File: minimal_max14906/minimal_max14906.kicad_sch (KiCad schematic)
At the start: 56 parts, among them Q1 SI7309DN-T1-E3, Q2 SI7309DN-T1-E3, Q3 SI7309DN-T1-E3, Q4 SI7309DN-T1-E3, U1 MAX14906ATM+

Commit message: minor updates
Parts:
- U1: MPN (none) -> MAX14906ATM+
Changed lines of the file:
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@@
+			)
+		)
+		(property "MPN" "MAX14906ATM+"
+			(at 167.64 152.4 0)
+			(effects
+				(font
+					(size 1.27 1.27)
+				)
+				(justify left)
+				(hide yes)
 			)
 		)

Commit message: Minor updates
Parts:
- added J1, J2, J3, J4: CLP-102-02-G-D-BE, connector_footprints:CLP-102-02-G-D-BE, symbol UNITED_CONNECTORS_DATA_BASE:J_CLP-102-02-G-D-BE
- added J5: CLP-114-02-G-D-BE, connector_footprints:CLP-114-02-G-D-BE, symbol UNITED_CONNECTORS_DATA_BASE:J_CLP-114-02-G-D-BE
- added J6, J7: CLP-104-02-G-D-BE, connector_footprints:CLP-104-02-G-D-BE, symbol UNITED_CONNECTORS_DATA_BASE:J_CLP-104-02-G-D-BE
- added TP25, TP26: TestPoint, test_point_footprints:TestPoint_THTPad_Castelated, symbol UNITED_TEST_POINTS:TestPoint_Castelated
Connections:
- net 3V3: now also J5.17, J5.18
- net CHANNEL_1: now also J4.3, J4.4
- net CHANNEL_2: now also J3.1, J3.2
- net CHANNEL_3: now also J2.3, J2.4
- net CHANNEL_4: now also J1.1, J1.2
- net CLK: now also J5.11, J5.12
- net D1: now also J5.25, J5.26
- net D2: now also J5.27, J5.28
- net D3: now also J5.1, J5.2
- net D4: now also J5.3, J5.4
- net EN: now also J5.21, J5.22
- net GNDA: now also J1.3, J1.4, J2.1, J2.2, J3.3, J3.4, J4.1, J4.2, J5.15, J5.16, J6.1, J6.2, J7.7, J7.8, TP26.1
- net SDI: now also J5.7, J5.8
- net SDO: now also J5.13, J5.14
- net SYNCH: now also J5.5, J5.6
- net VDD_24V_MAX14906: now also J6.3, J6.4, J7.5, J7.6, TP25.1
- net ~{CS}: now also J5.10, J5.9
- net ~{FAULT}: now also J5.19, J5.20
- net ~{READY}: now also J5.23, J5.24
- no-connect marks 1 -> 9
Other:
- moved on the sheet: C1, C10, C11, C12, C13, C2, C3, C4, C5, C6, C7, C8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

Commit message: Update subproject commit for KiCAD Symbol Generator
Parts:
- renumbered C5 to C1, C12 to C10, C7 to C11, C6 to C12, C9 to C13, C8 to C2, C2 to C3, C13 to C4, C4 to C5, C11 to C6, C3 to C7, C10 to C8, C1 to C9, D9 to D1, D8 to D2, D4 to D3, D7 to D4, D3 to D5, D2 to D7, D5 to D8, D1 to D9, J5 to J1, J7 to J4, J6 to J5, J1 to J6, J4 to J7, Q2 to Q1, Q4 to Q2, Q1 to Q3, Q3 to Q4, R5 to R1, R4 to R2, R2 to R4, R1 to R5, TP12 to TP1, TP8 to TP10, TP9 to TP11, TP10 to TP12, TP14 to TP13, TP13 to TP14, TP22 to TP15, TP23 to TP16, TP19 to TP17, TP25 to TP19, TP11 to TP2, TP15 to TP20, TP26 to TP21, TP16 to TP22, TP20 to TP23, TP17 to TP24, TP21 to TP25, TP24 to TP26, TP7 to TP3, TP6 to TP4, TP4 to TP6, TP3 to TP7, TP2 to TP8, TP1 to TP9

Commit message: Minor updates to project files
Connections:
- net 3V3: no longer J1.17
- net CLK: no longer J1.11
- net D1: no longer J1.25
- net D2: no longer J1.27
- net D3: no longer J1.1
- net D4: no longer J1.3
- net EN: no longer J1.21
- net GNDA: now also J1.1, J1.11, J1.13, J1.17, J1.19, J1.21, J1.23, J1.25, J1.27, J1.3, J1.5, J1.7, J1.9
- net SDI: no longer J1.7
- net SDO: no longer J1.13
- net SYNCH: no longer J1.5
- net ~{CS}: no longer J1.9
- net ~{FAULT}: no longer J1.19
- net ~{READY}: no longer J1.23

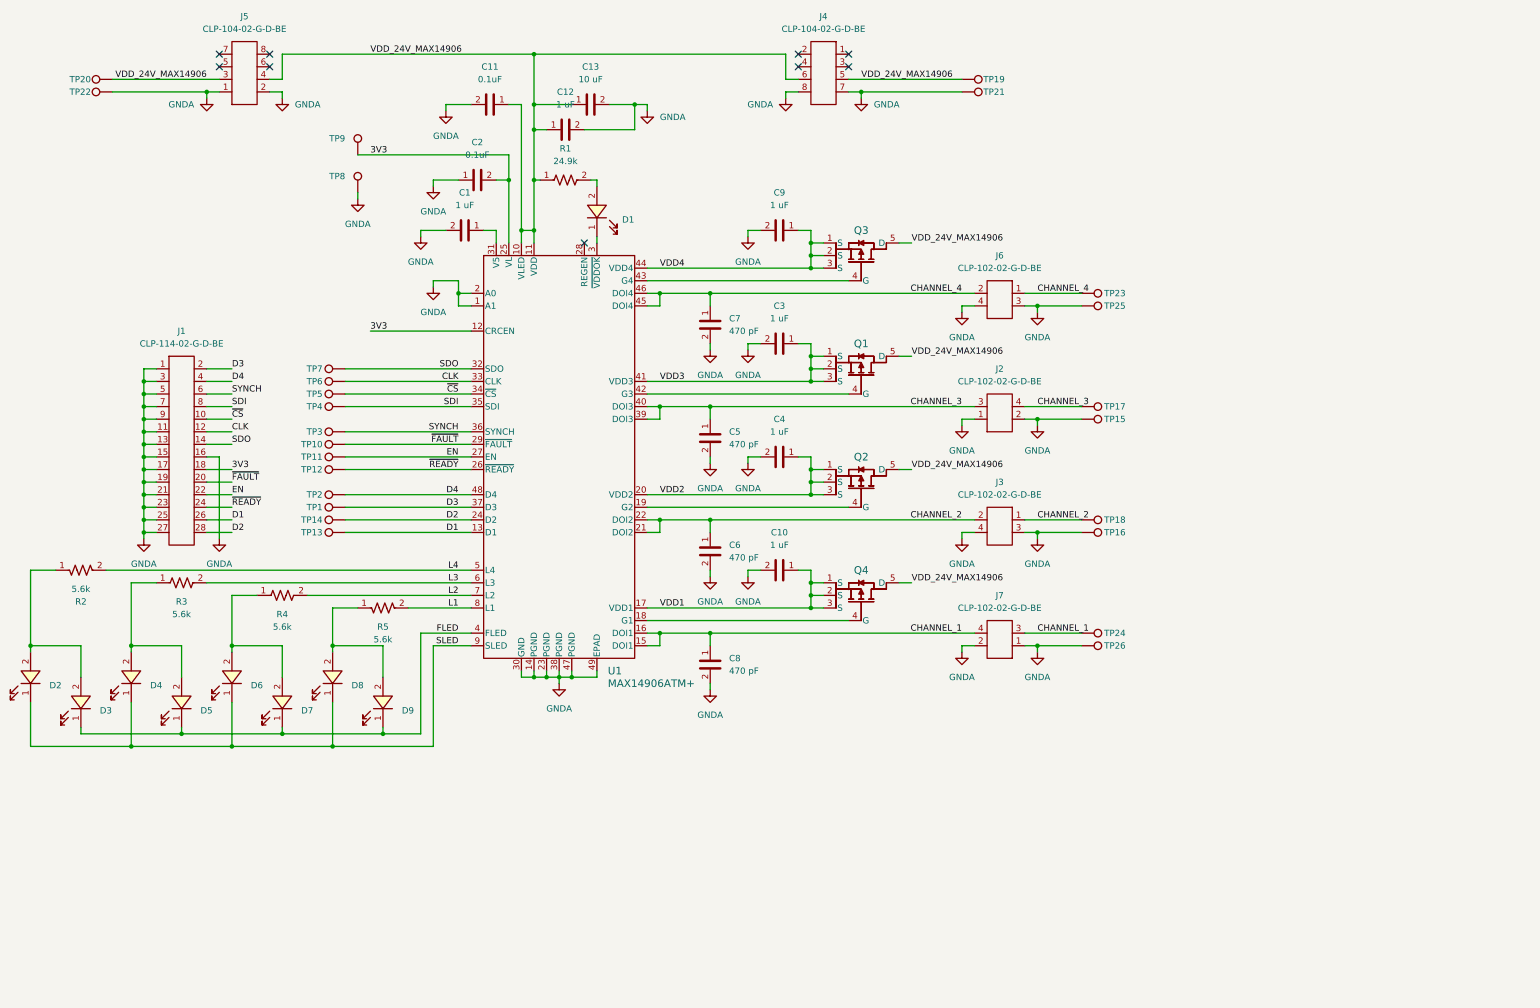
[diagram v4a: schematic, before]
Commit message: Update KiCAD Symbol Generator and configuration files
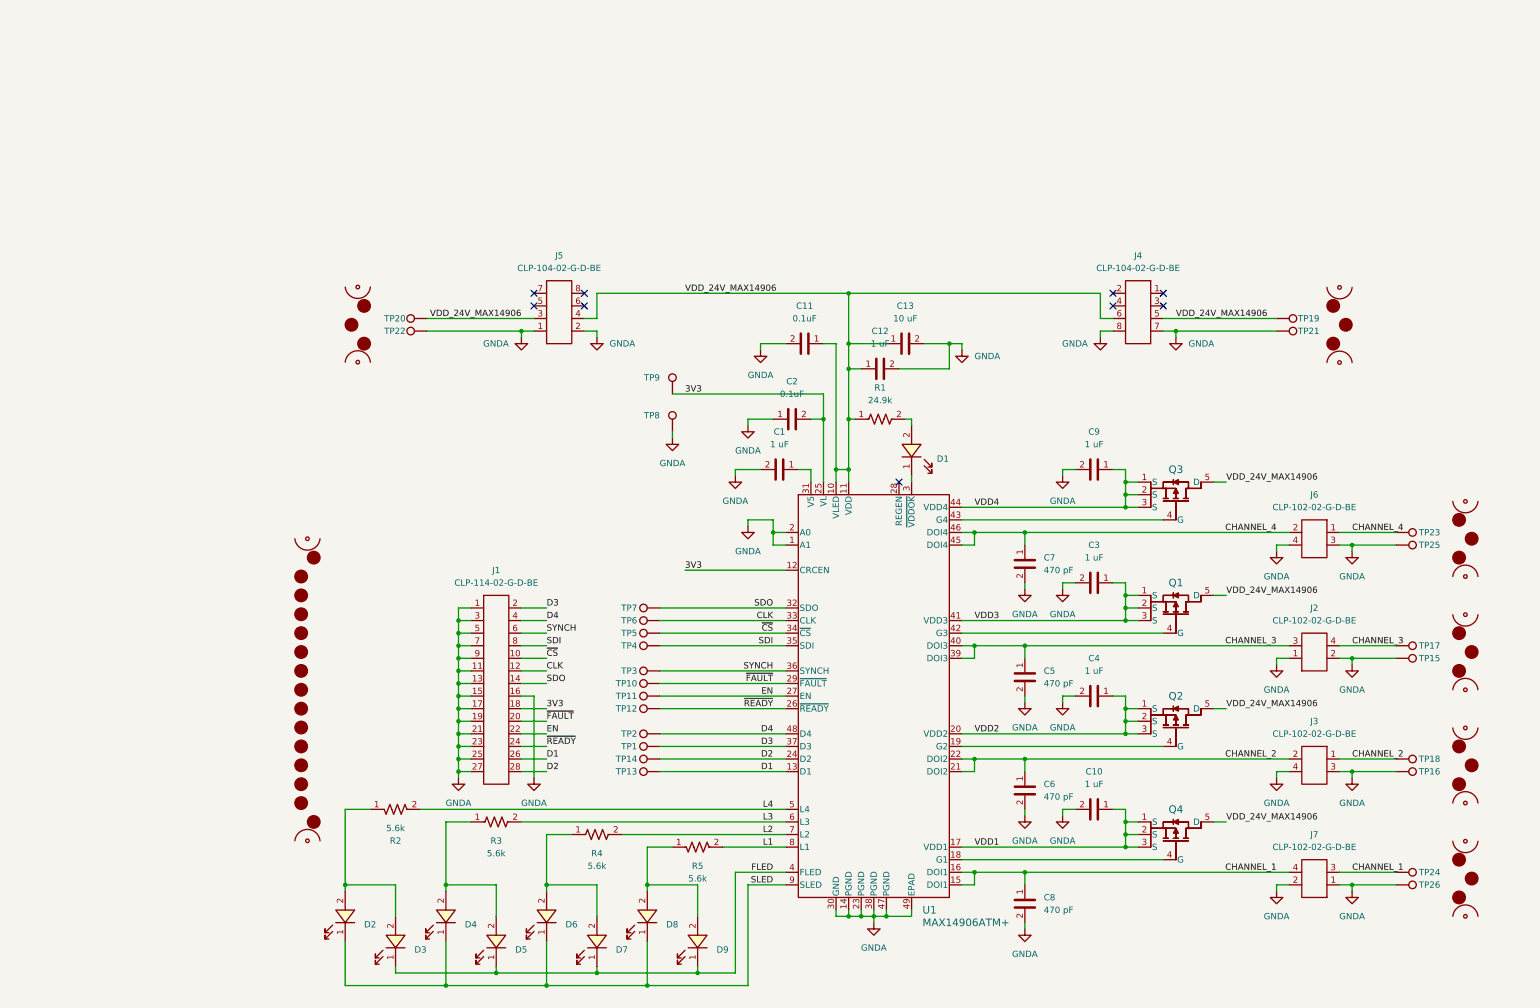
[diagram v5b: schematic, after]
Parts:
- added MB1, MB2, MB3, MB4, MB6, MB7: mouse-bite-midle-50mil-200mil, mouse_bite_footprints:mouse-bite-midle-50mil-200mil, symbol UNITED_MOUSE_BITES_DATA_BASE:mouse-bite-midle-50mil-200mil
- added MB5: mouse-bite-midle-50mil-200mil, mouse_bite_footprints:mouse-bite-50mil-790mil, symbol UNITED_MOUSE_BITES_DATA_BASE:mouse-bite-50mil-790mil
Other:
- moved on the sheet: C1, C10, C11, C12, C13, C2, C3, C4, C5, C6, C7, C8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

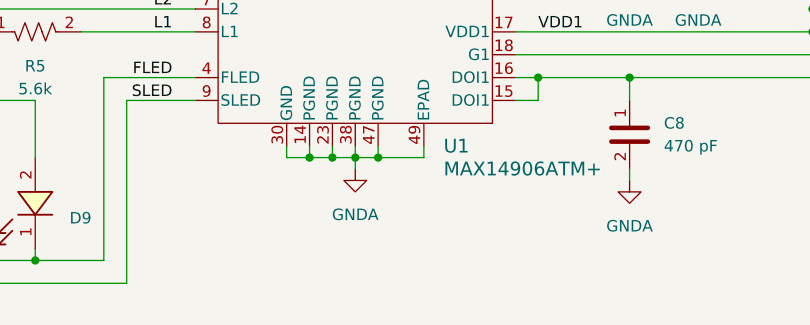
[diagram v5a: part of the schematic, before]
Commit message: Update KiCAD Symbol Generator subproject and add new footprints for fiducial markers
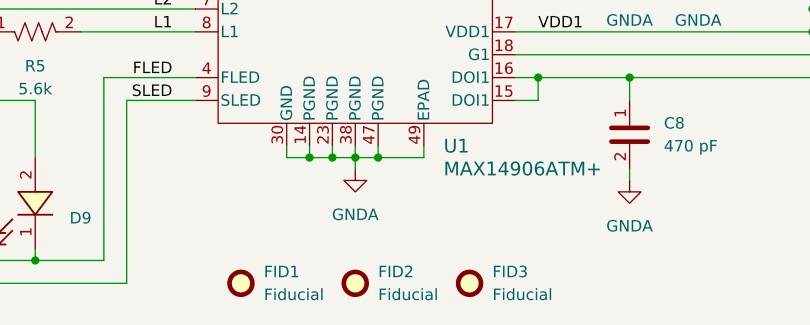
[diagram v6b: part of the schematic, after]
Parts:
- added FID1, FID2, FID3: Fiducial, no_components_footprints:Fiducial_0.5mm_Mask1mm, symbol UNITED_NO_COMPONENTS_DATA_BASE:Fiducial
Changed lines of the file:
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@@
 	)
 	(symbol
+		(lib_id "UNITED_NO_COMPONENTS_DATA_BASE:Fiducial")
+		(at 228.6 210.82 0)
+		(unit 1)
+		(exclude_from_sim no)
+		(in_bom yes)
+		(on_board yes)
+		(dnp no)
+		(fields_autoplaced yes)
+		(property "Reference" "FID3"
+			(at 231.14 209.5499 0)
+			(effects
+				(font
+					(size 1.27 1.27)
+				)
+				(justify left)
+			)
+		)
+		(property "Value" "Fiducial"
+			(at 231.14 212.0899 0)
+			(effects
+				(font
+					(size 1.27 1.27)
+				)
+				(justify left)
+			)
+		)
+		(property "Footprint" "no_components_footprints:Fiducial_0.5mm_Mask1mm"
+			(at 228.6 218.44 0)
+			(effects
+				(font
+					(size 1.27 1.27)
+				)
+				(justify left)
+				(hide yes)
+			)
+		)
+		(property "Datasheet" "~"
+			(at 228.6 213.36 0)
+			(effects
+				(font
+					(size 1.27 1.27)
+				)
+				(justify left)
+				(hide yes)
+			)
+		)
+		(property "Description" "Fiducial Marker"
+			(at 228.6 215.9 0)
+			(effects
+				(font
+					(size 1.27 1.27)
+				)
+				(justify left)
+				(hide yes)
+			)
+		)
+		(instances
+			(project "minimal_max14906"
+				(path "/0138bc01-efaa-4f20-bf65-043bbc1a8346"
+					(reference "FID3")
+					(unit 1)
+				)
+			)
+		)
+	)
+	(symbol
 		(lib_id "UNITED_DIODES_DATA_BASE:D_APHHS1005CGCK")
 		(at 109.22 196.85 90)
@@
 	)
 	(symbol
+		(lib_id "UNITED_NO_COMPONENTS_DATA_BASE:Fiducial")
+		(at 215.9 210.82 0)
+		(unit 1)
+		(exclude_from_sim no)
+		(in_bom yes)
+		(on_board yes)
+		(dnp no)
+		(fields_autoplaced yes)
+		(property "Reference" "FID2"
+			(at 218.44 209.5499 0)
+			(effects
+				(font
+					(size 1.27 1.27)
+				)
+				(justify left)
+			)
+		)
+		(property "Value" "Fiducial"
+			(at 218.44 212.0899 0)
+			(effects
+				(font
+					(size 1.27 1.27)
+				)
+				(justify left)
+			)
+		)
+		(property "Footprint" "no_components_footprints:Fiducial_0.5mm_Mask1mm"
+			(at 215.9 218.44 0)
+			(effects
+				(font
+					(size 1.27 1.27)
+				)
+				(justify left)
+				(hide yes)
+			)
+		)
+		(property "Datasheet" "~"
+			(at 215.9 213.36 0)
+			(effects
+				(font
+					(size 1.27 1.27)
+				)
+				(justify left)
+				(hide yes)
+			)
+		)
+		(property "Description" "Fiducial Marker"
+			(at 215.9 215.9 0)
+			(effects
+				(font
+					(size 1.27 1.27)
+				)
+				(justify left)
+				(hide yes)
+			)
+		)
+		(instances
+			(project "minimal_max14906"
+				(path "/0138bc01-efaa-4f20-bf65-043bbc1a8346"
+					(reference "FID2")
+					(unit 1)
+				)
+			)
+		)
+	)
+	(symbol
 		(lib_id "power:GNDA")
 		(at 297.18 146.05 0)
@@
 					(unit 1)
 				)
+			)
+		)
+	)
+	(symbol
+		(lib_id "UNITED_NO_COMPONENTS_DATA_BASE:Fiducial")
+		(at 203.2 210.82 0)
+		(unit 1)
+		(exclude_from_sim no)
+		(in_bom yes)
+		(on_board yes)
+		(dnp no)
+		(fields_autoplaced yes)
+		(property "Reference" "FID1"
+			(at 205.74 209.5499 0)
+			(effects
+				(font
+					(size 1.27 1.27)
+				)
+				(justify left)
+			)
+		)
+		(property "Value" "Fiducial"
+			(at 205.74 212.0899 0)
+			(effects
+				(font
+					(size 1.27 1.27)
+				)
+				(justify left)
+			)
+		)
+		(property "Footprint" "no_components_footprints:Fiducial_0.5mm_Mask1mm"
+			(at 203.2 218.44 0)
+			(effects
+				(font
+					(size 1.27 1.27)
+				)
+				(justify left)
+				(hide yes)
+			)
+		)
+		(property "Datasheet" "~"
+			(at 203.2 213.36 0)
+			(effects
+				(font
+					(size 1.27 1.27)
+				)
+				(justify left)
+				(hide yes)
+			)
+		)
+		(property "Description" "Fiducial Marker"
+			(at 203.2 215.9 0)
+			(effects
+				(font
+					(size 1.27 1.27)
+				)
+				(justify left)
+				(hide yes)
+			)
+		)
+		(instances
+			(project ""
+				(path "/0138bc01-efaa-4f20-bf65-043bbc1a8346"
+					(reference "FID1")
+					(unit 1)
+				)

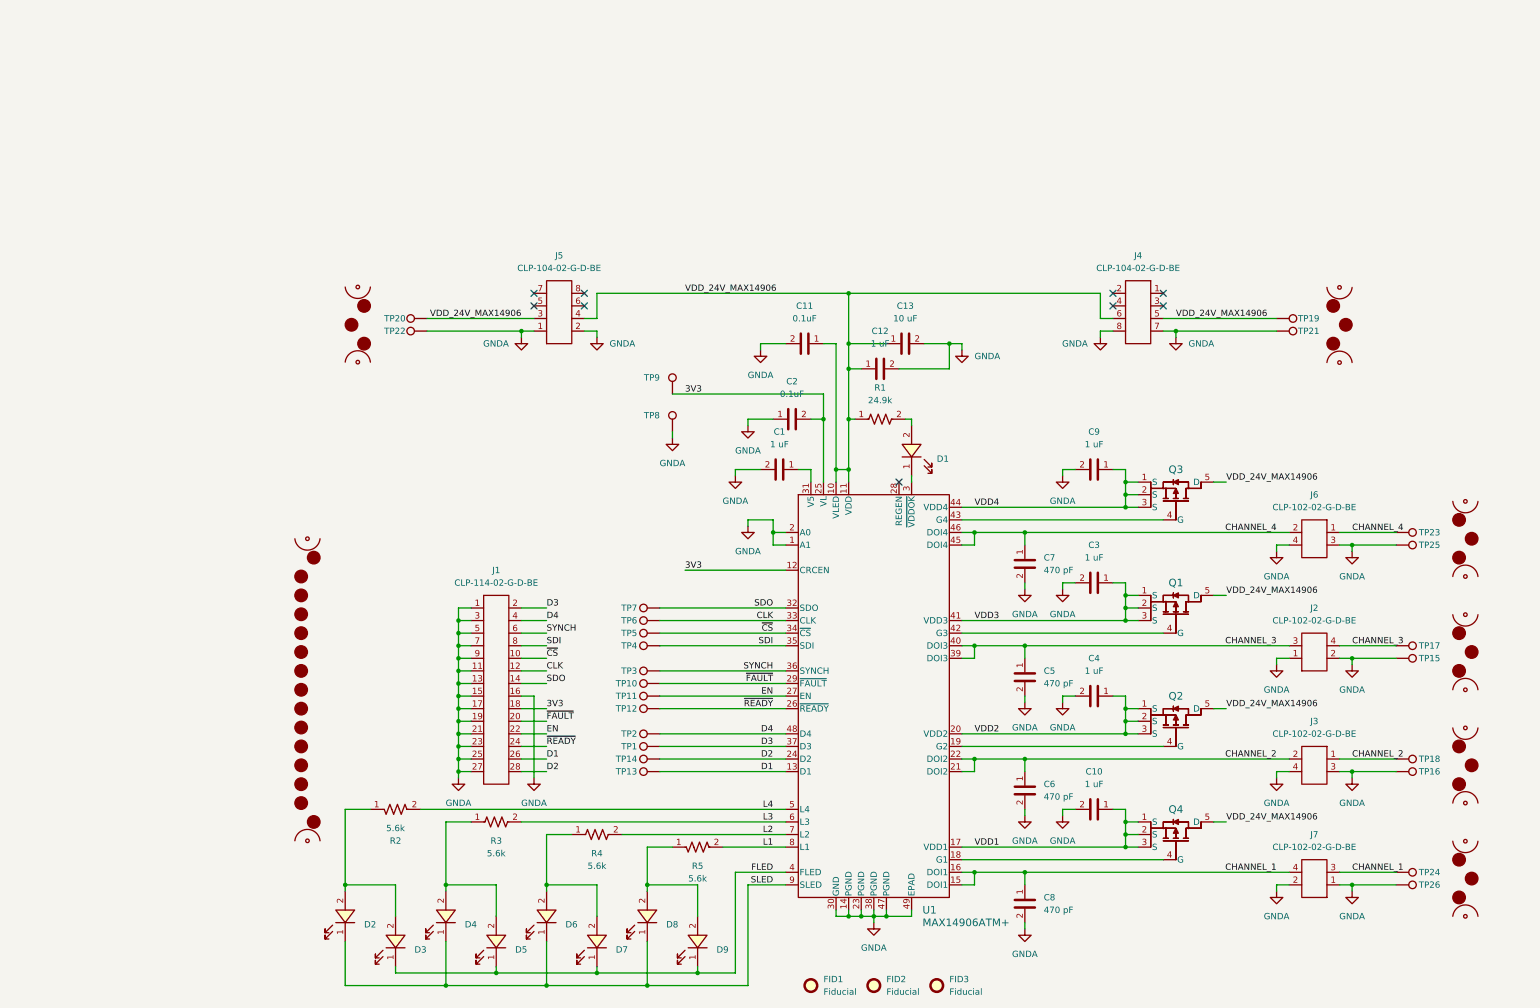
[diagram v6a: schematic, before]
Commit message: Update KiCAD Symbol Generator with new features and improvements
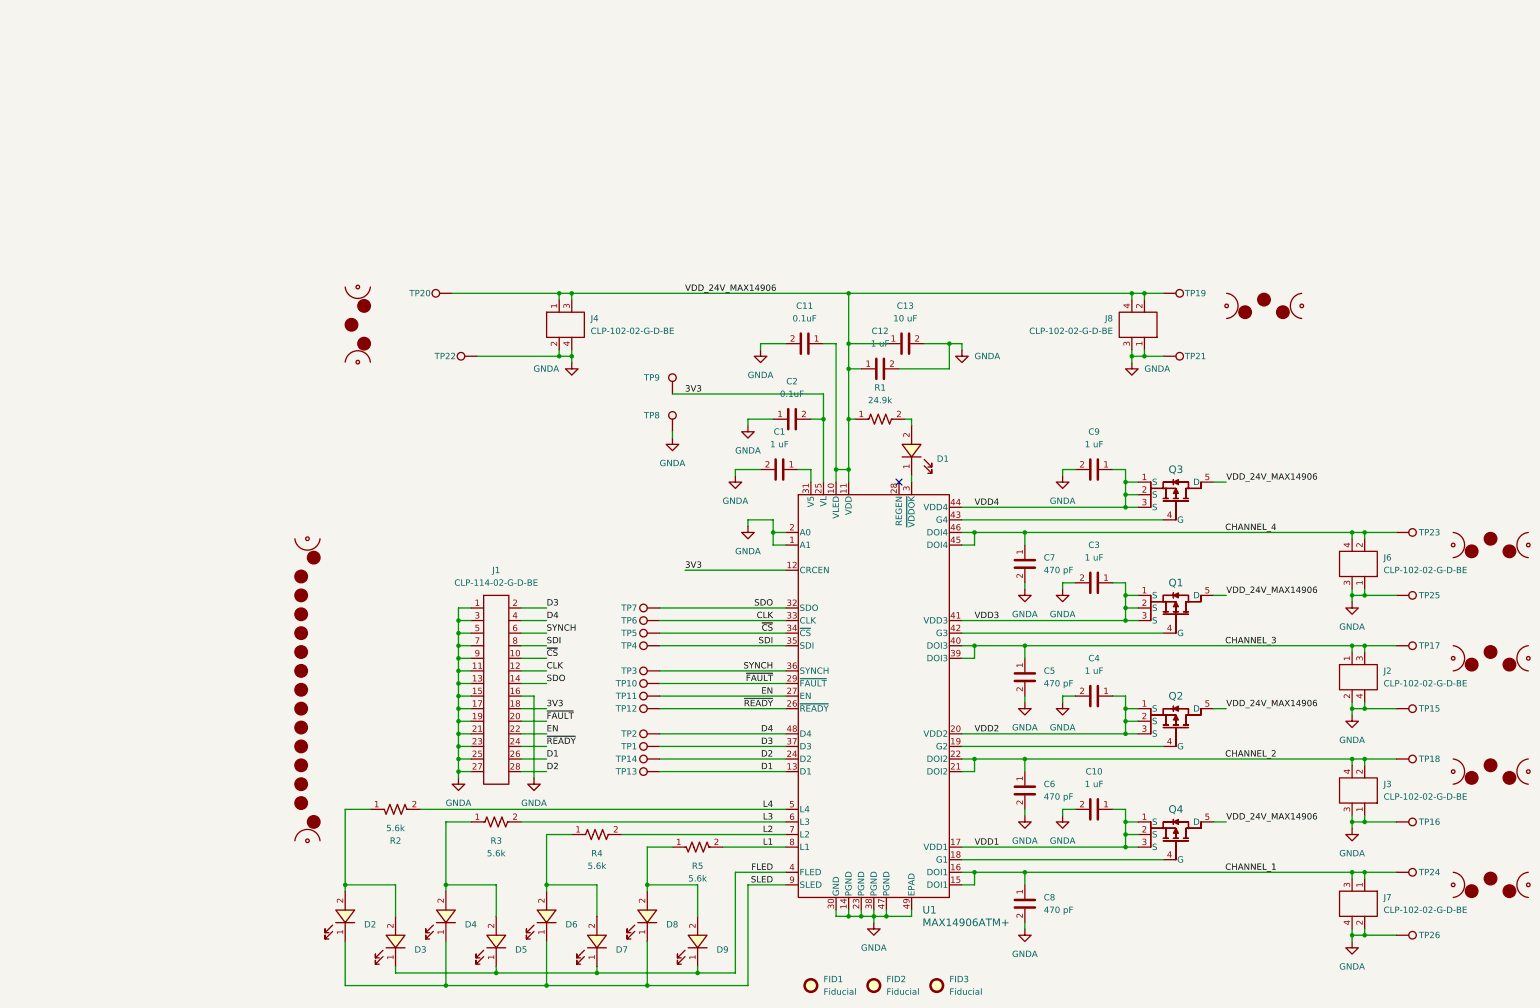
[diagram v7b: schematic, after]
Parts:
- removed J4, J5: CLP-104-02-G-D-BE, connector_footprints:CLP-104-02-G-D-BE, symbol UNITED_CONNECTORS_DATA_BASE:J_CLP-104-02-G-D-BE
- added J4, J8: CLP-102-02-G-D-BE, connector_footprints:CLP-102-02-G-D-BE, symbol UNITED_CONNECTORS_DATA_BASE:J_CLP-102-02-G-D-BE
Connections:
- net CHANNEL_1: now also J7.1; no longer J7.4
- net CHANNEL_2: now also J3.4; no longer J3.1
- net CHANNEL_3: now also J2.1; no longer J2.4
- net CHANNEL_4: now also J6.4; no longer J6.1
- net GNDA: now also J2.4, J3.1, J6.1, J7.4, J4.2, J4.4, J8.1, J8.3; no longer J2.1, J3.4, J6.4, J7.1
- net VDD_24V_MAX14906: now also J4.1, J4.3, J8.2, J8.4
- no-connect marks 9 -> 1
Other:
- moved on the sheet: J2, J3, J6, J7, TP15, TP16, TP19, TP20, TP21, TP22, TP25, TP26
